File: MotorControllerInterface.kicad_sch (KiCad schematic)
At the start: 0 parts

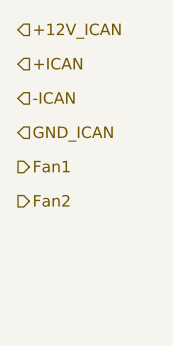
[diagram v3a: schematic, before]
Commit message: Updated Controls + Telemetry
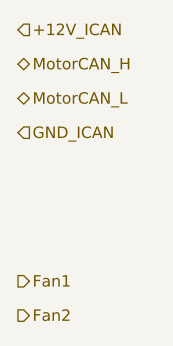
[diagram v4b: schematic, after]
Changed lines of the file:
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@@
 	(generator_version "9.0")
 	(paper "A4")
-	(hierarchical_label "-ICAN"
-		(shape input)
-		(at 147.32 102.87 0)
-		(effects
-			(font
-				(size 1.27 1.27)
-			)
-			(justify left)
-		)
-	)
 	(hierarchical_label "+12V_ICAN"
 		(shape input)
@@
 	(hierarchical_label "Fan1"
 		(shape output)
-		(at 147.32 110.49 0)
+		(at 147.32 123.19 0)
 		(effects
 			(font
@@
 	(hierarchical_label "Fan2"
 		(shape output)
-		(at 147.32 114.3 0)
+		(at 147.32 127 0)
 		(effects
 			(font
@@
 		)
 	)
-	(hierarchical_label "+ICAN"
-		(shape input)
+	(hierarchical_label "MotorCAN_H"
+		(shape bidirectional)
 		(at 147.32 99.06 0)
 		(effects
@@
 		(effects
 			(font
+				(size 1.27 1.27)
+			)
+			(justify left)
+		)
+	)
+	(hierarchical_label "MotorCAN_L"
+		(shape bidirectional)
+		(at 147.32 102.87 0)
+		(effects
+			(font
